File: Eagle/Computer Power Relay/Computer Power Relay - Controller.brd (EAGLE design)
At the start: 34.4 x 52.6 mm, 38 parts, among them U1 RP2040, U2 AP2112M-3.3TRG1

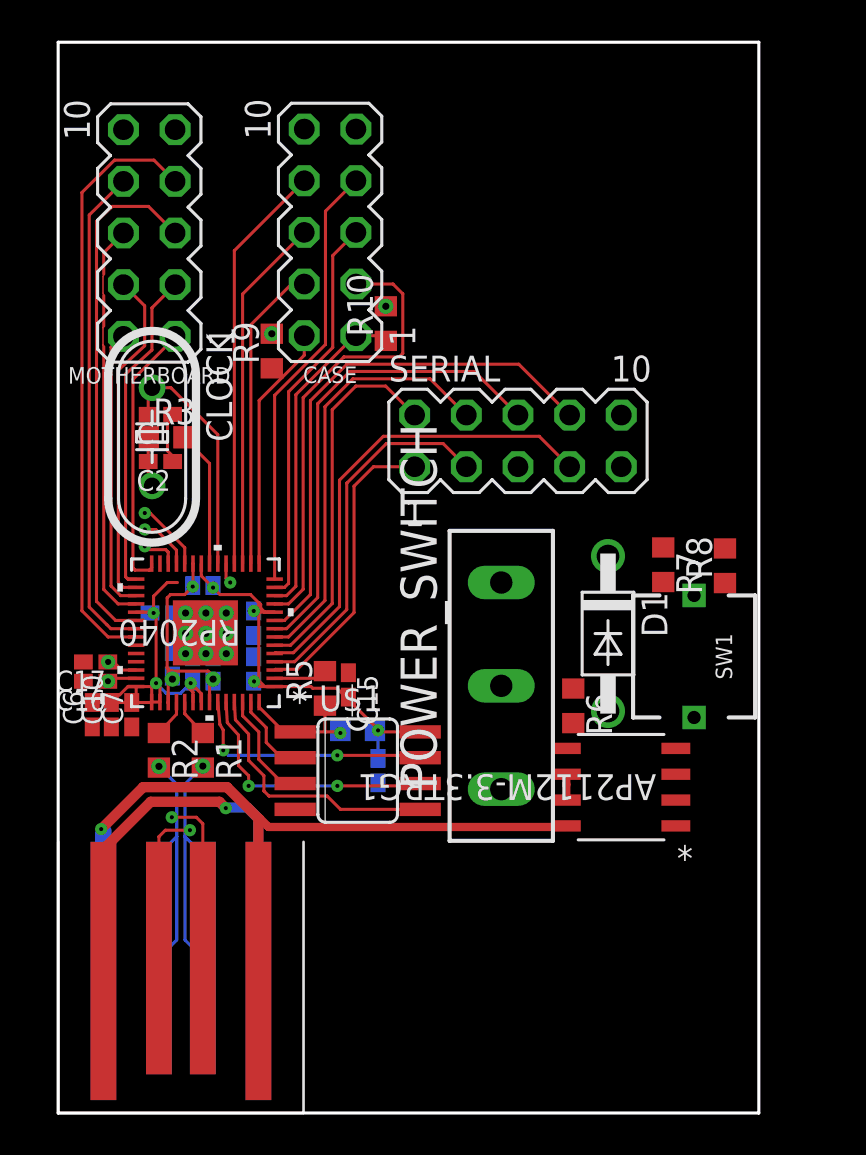
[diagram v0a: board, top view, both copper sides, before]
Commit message: Split controller from power splitter
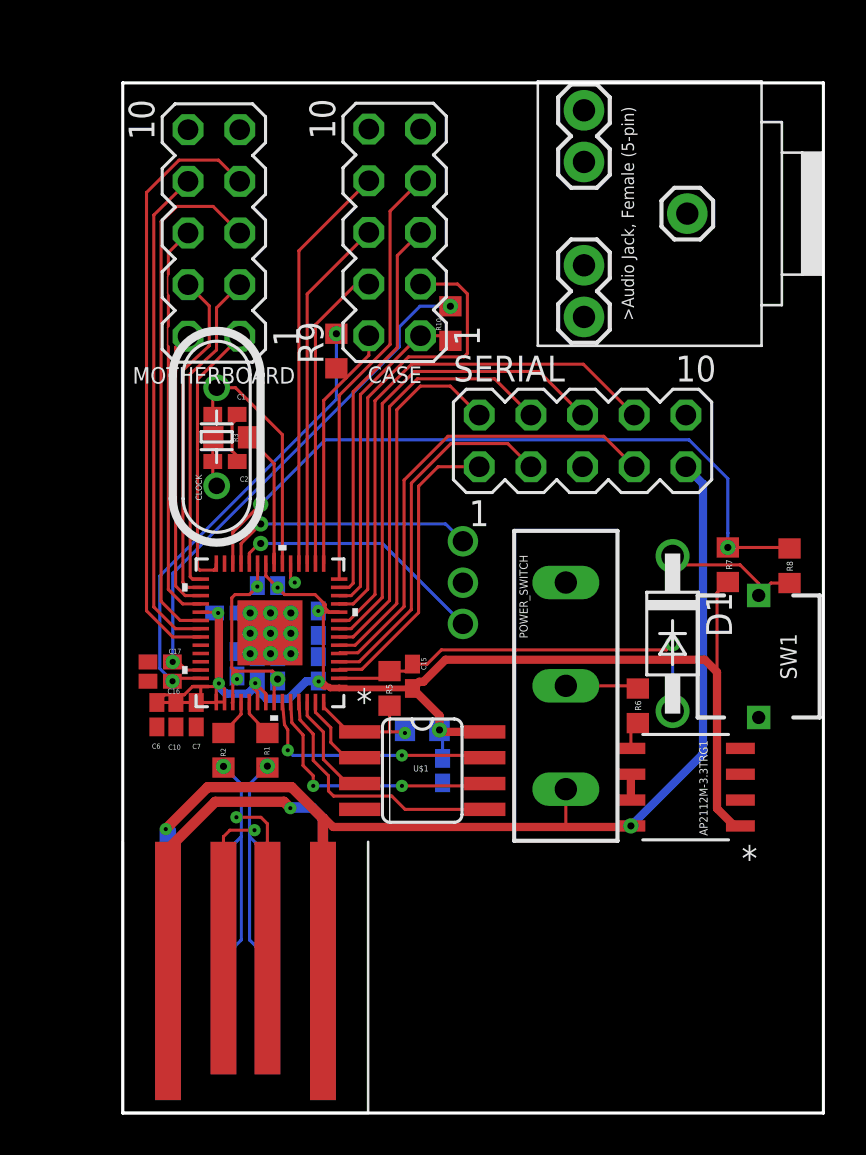
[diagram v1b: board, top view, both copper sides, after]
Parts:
- added U$3: AUDIO_JACK_FEMALE_5-PIN, Inventory:AUDIO_JACK_FEMALE_5-PIN
- moved C15 3.18 mm to (14.2, 21.5)
- moved C11 3.18 mm to (15.7, 16.8)
- moved D1 3.18 mm to (27.0, 23.6)
- moved MOTHERBOARD 3.18 mm to (4.48, 43.3)
- moved POWER_SWITCH 3.18 mm to (21.8, 21.0)
- moved R4 3.18 mm to (14.7, 18.8)
- moved R6 3.18 mm to (25.3, 20.0)
- moved R7 3.18 mm to (29.8, 27.0)
- moved R8 3.18 mm to (32.8, 26.9)
- moved SERIAL 3.18 mm to (22.6, 33.0)
- moved SW1 3.18 mm to (31.3, 22.4)
- moved U$1 3.18 mm to (14.7, 16.8)
- moved C1 3.18 mm to (5.03, 34.4)
- moved C10 3.18 mm to (2.62, 19.6)
- moved C12 3.18 mm to (5.62, 22.1)
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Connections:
- net N$7 renamed SWITCH
- net N$8 renamed BUTTON
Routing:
- net RUN: track 1.83 -> 35.0 mm, vias 1 -> 2
- net 3V3: track 43.4 -> 75.3 mm
- net PWM0: track 1.54 -> 25.6 mm
- net 5V: track 39.1 -> 60.4 mm, vias 1 -> 2
- net PWM1: track 1.45 -> 22.4 mm
- net BOOTSEL: track 2.62 -> 20.4 mm, vias 0 -> 1
- net DBG-DIO: track 2.64 -> 12.6 mm, vias 1 -> 2
- net DBG-CLK: track 3.45 -> 12.8 mm, vias 1 -> 2
- net BUTTON: track 0.00 -> 7.15 mm
- net SWITCH: track 0.00 -> 3.59 mm
- net EN: track 0.00 -> 1.39 mm
- net GND: vias 11 -> 12
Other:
- board size 34.4 x 52.6 mm -> 34.5 x 50.6 mm

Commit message: Beginning Merge of Boards (Relay)
I'm beginning to merge the Controller and Power Strip boards into one so that I can print it for cheaper.
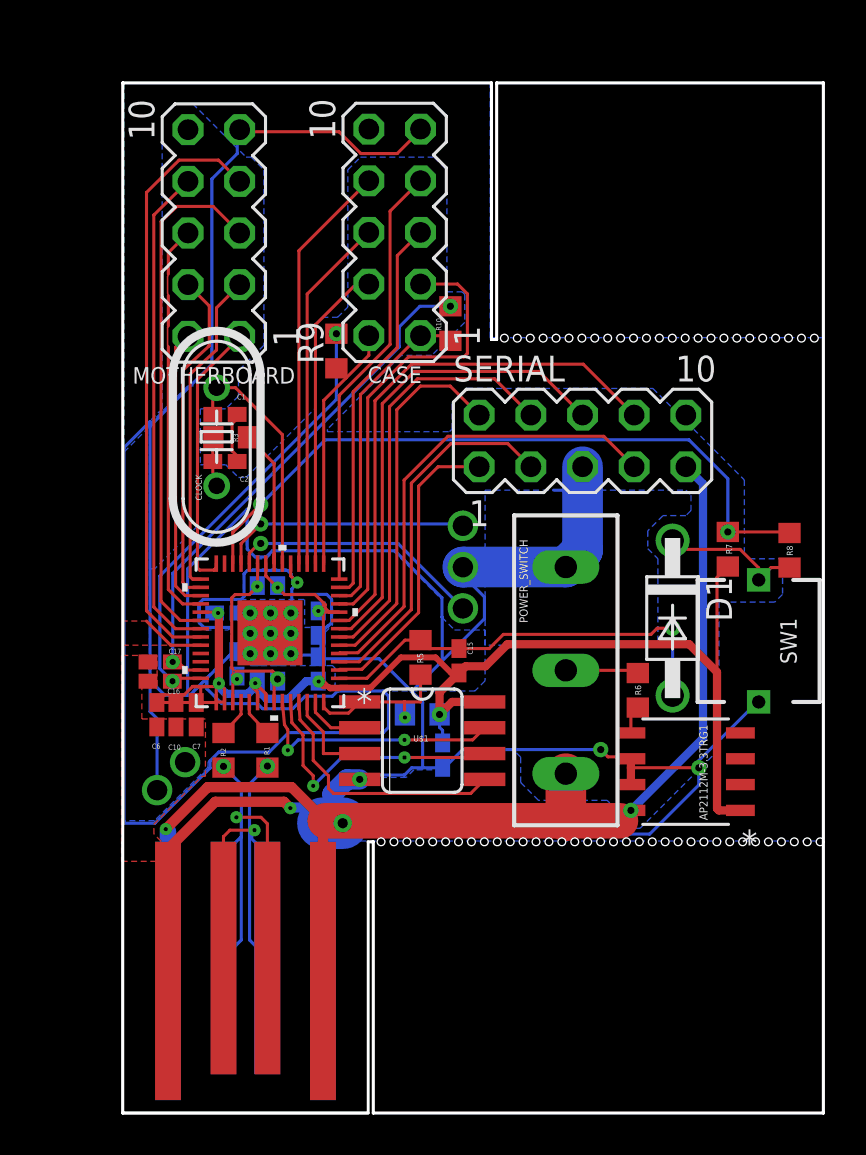
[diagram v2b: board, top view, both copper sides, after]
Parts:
- removed U$3: AUDIO_JACK_FEMALE_5-PIN, Inventory:AUDIO_JACK_FEMALE_5-PIN
- moved C15 2.41 mm to (16.5, 22.2)
- moved R5 2.16 mm to (14.6, 22.4)
- moved U$1 1.47 mm to (14.7, 18.3)
- moved C11 0.76 mm to (15.7, 17.6)
- moved POWER_SWITCH 0.76 mm to (21.8, 21.8)
- moved R4 0.76 mm to (14.7, 19.6)
- moved R6 0.76 mm to (25.3, 20.8)
- moved R7 0.76 mm to (29.8, 27.7)
- moved R8 0.76 mm to (32.8, 27.7)
- moved SW1 0.76 mm to (31.3, 23.2)
- moved U2 0.76 mm to (27.7, 16.8)
- moved D1 0.76 mm to (27.0, 24.3)
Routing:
- net GND: track 27.4 -> 259.8 mm, vias 12 -> 18
- net GPIO25: track 0.00 -> 3.16 mm
- net 3V3: track 75.3 -> 76.9 mm
- net QSPI_SS_N: track 6.28 -> 7.62 mm
- net N$17: track 4.03 -> 2.99 mm
- net D+: track 18.3 -> 19.3 mm
- net D-: track 19.1 -> 20.0 mm
- net N$16: track 5.43 -> 4.65 mm
- net RUN: track 35.0 -> 34.2 mm
- net BOOTSEL: track 20.4 -> 21.1 mm
- net 1V1: track 12.4 -> 11.8 mm
- net N$19: track 13.0 -> 13.6 mm
- added copper zone on layer 1, net 1V1
- added copper zone on layer 1, net GND
- added copper zone on layer 16, net GND
- added copper zone on layer 1, net GPIO25
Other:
- outline, holes or cut-outs redrawn
